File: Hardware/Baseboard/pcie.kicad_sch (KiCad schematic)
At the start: 1 part, among them J1 2199230-4

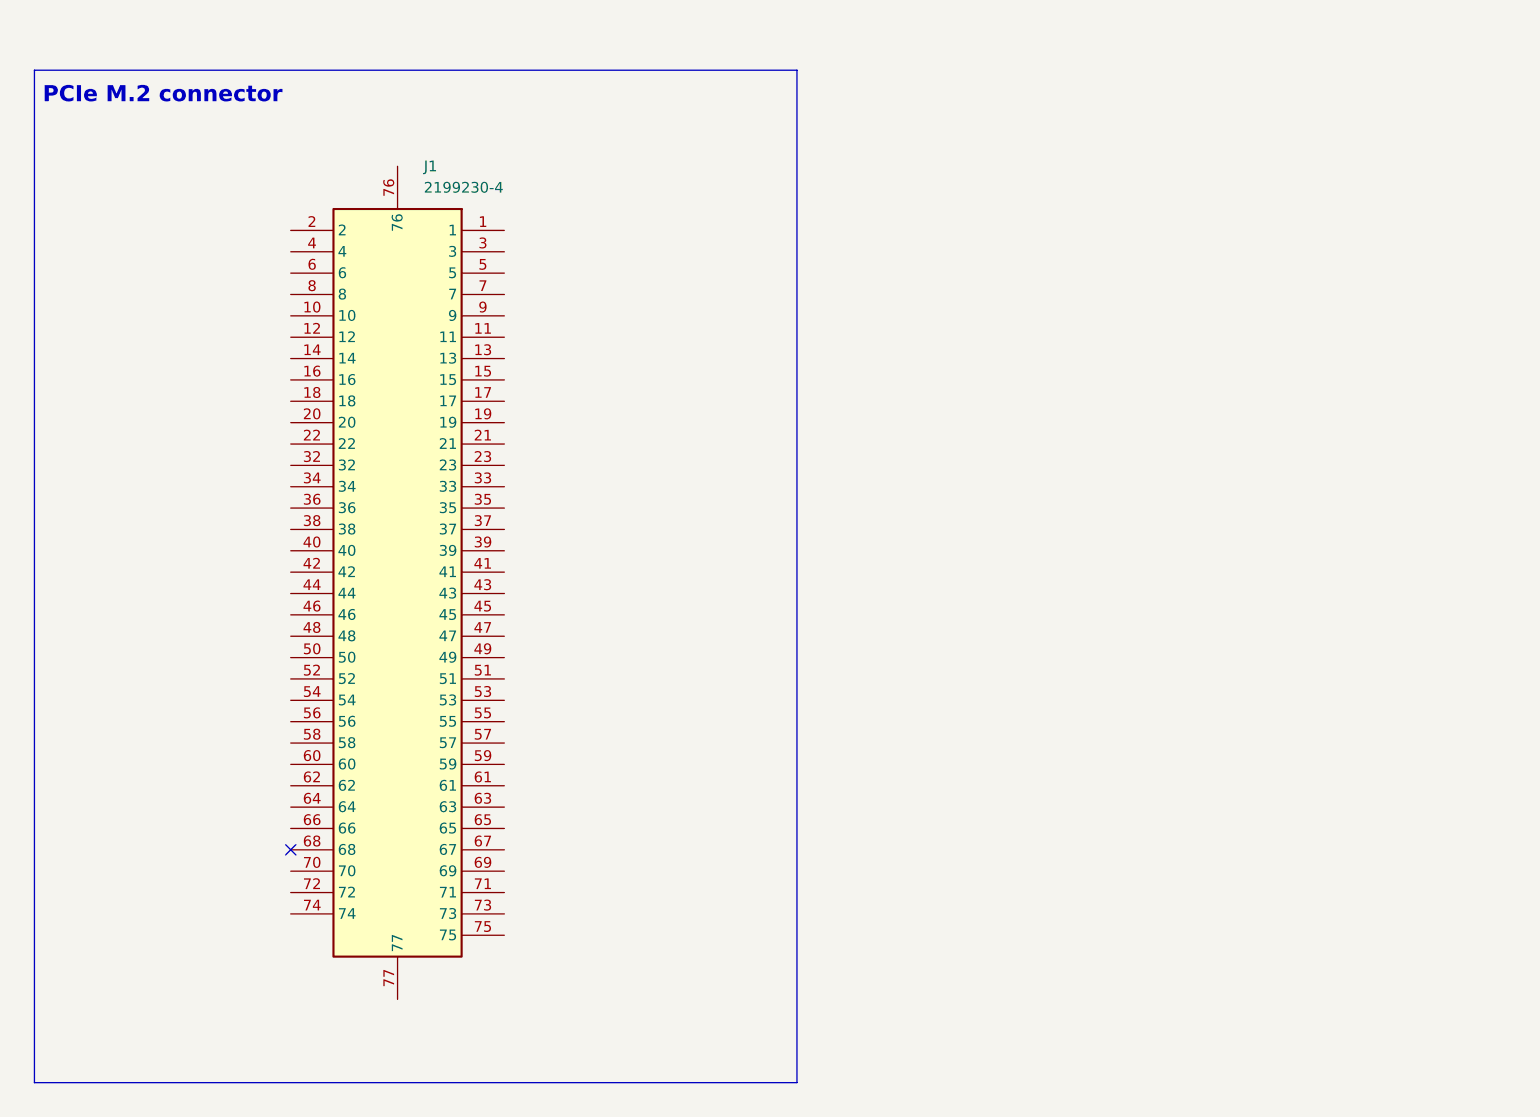
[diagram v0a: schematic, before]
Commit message: PCIe M.2 connector changed
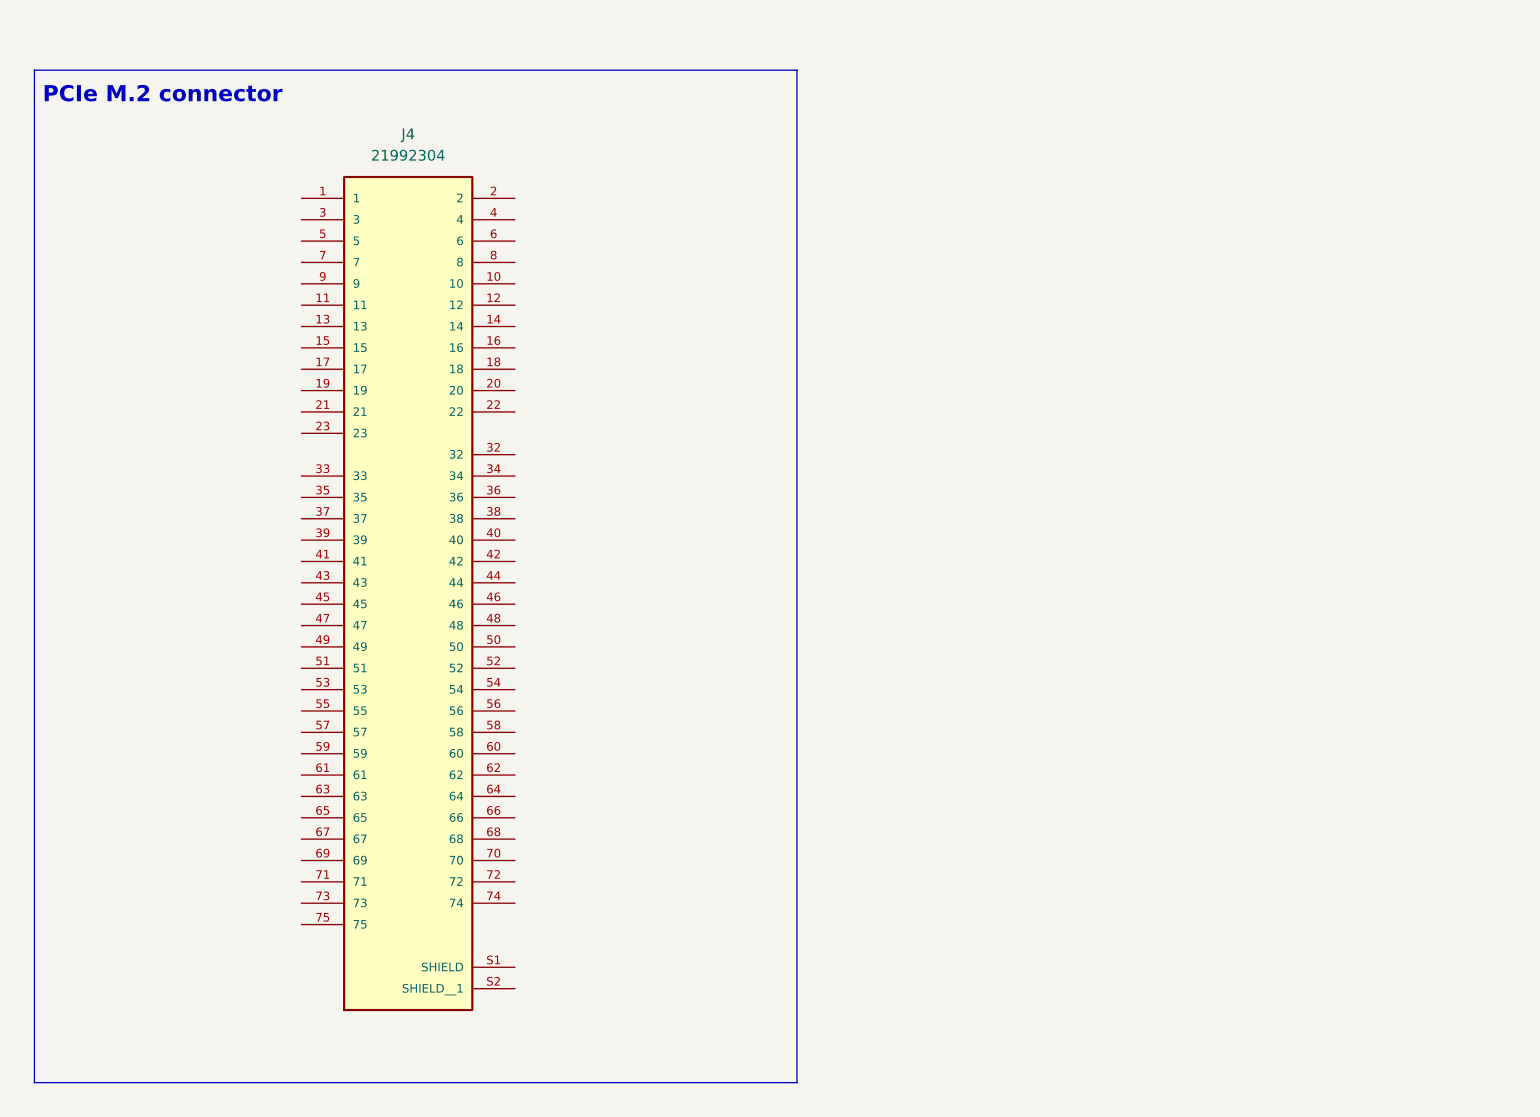
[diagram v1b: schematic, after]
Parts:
- removed J1: 2199230-4, FPGA4RISCV:21992304, symbol FPGA4RISCV:2199230-4
- added J4: 21992304, FPGA4RISCV:TE_21992304, symbol FPGA4RISCV:21992304
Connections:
- no-connect marks 1 -> 0
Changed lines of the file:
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@@
 		)
-	)
-	(no_connect
-		(at 78.74 125.73)
 	)
 	(symbol
-		(lib_id "FPGA4RISCV:2199230-4")
-		(at 91.44 44.45 270)
+		(lib_id "FPGA4RISCV:21992304")
+		(at 92.71 93.98 0)
 		(unit 1)
 		(exclude_from_sim no)
@@
 		(dnp no)
 		(fields_autoplaced yes)
-		(property "Reference" "J1"
-			(at 94.5581 44.45 90)
-			(effects
-				(font
-					(size 1.27 1.27)
-				)
-				(justify left)
-			)
-		)
-		(property "Value" "2199230-4"
-			(at 94.5581 46.99 90)
-			(effects
-				(font
-					(size 1.27 1.27)
-				)
-				(justify left)
-			)
-		)
-		(property "Footprint" "FPGA4RISCV:21992304"
-			(at 1.6 139.7 0)
-			(effects
-				(font
-					(size 1.27 1.27)
-				)
-				(justify left top)
-				(hide yes)
-			)
-		)
-		(property "Datasheet" "https://www.te.com/commerce/DocumentDelivery/DDEController?Action=srchrtrv&DocNm=1-1773706-1NGFF_QRG-SC&DocType=Data%20Sheet&DocLang=Chinese (Simplified)&PartCntxt=2199230-4&DocFormat=pdf"
-			(at -98.4 139.7 0)
-			(effects
-				(font
-					(size 1.27 1.27)
-				)
-				(justify left top)
-				(hide yes)
-			)
-		)
-		(property "Description" "Body Features: Primary Product Color Black | Connector & Keying Code E | Configuration Features: Number of Positions 67 | PCB Mount Orientation Right Angle | Number of Rows 2 | Contact Features: PCB Contact Termination Area Plating Material Tin | Contact Mating Area Plating Material Gold | Contact Mating Area Plating Material Thickness 15 MICIN | PCB Contact Termination Area Plating Material Finish Matte | PCB Contact Termination Area Plating Material Gold Flash | Contact Base Material Copper Alloy | Contac"
-			(at 91.44 44.45 0)
-			(effects
-				(font
-					(size 1.27 1.27)
-				)
-				(hide yes)
-			)
-		)
-		(property "Height" ""
-			(at -298.4 139.7 0)
-			(effects
-				(font
-					(size 1.27 1.27)
-				)
-				(justify left top)
-				(hide yes)
-			)
-		)
-		(property "Mouser Part Number" "571-2199230-4"
-			(at -398.4 139.7 0)
-			(effects
-				(font
-					(size 1.27 1.27)
-				)
-				(justify left top)
-				(hide yes)
-			)
-		)
-		(property "Mouser Price/Stock" "https://www.mouser.co.uk/ProductDetail/TE-Connectivity/2199230-4?qs=EQCnRgr4b6HnhitEoflgGQ%3D%3D"
-			(at -498.4 139.7 0)
-			(effects
-				(font
-					(size 1.27 1.27)
-				)
-				(justify left top)
-				(hide yes)
-			)
-		)
-		(property "Manufacturer_Name" "TE Connectivity"
-			(at -598.4 139.7 0)
-			(effects
-				(font
-					(size 1.27 1.27)
-				)
-				(justify left top)
-				(hide yes)
-			)
-		)
-		(property "Manufacturer_Part_Number" "2199230-4"
-			(at -698.4 139.7 0)
-			(effects
-				(font
-					(size 1.27 1.27)
-				)
-				(justify left top)
-				(hide yes)
-			)
+		(property "Reference" "J4"
+			(at 92.71 40.64 0)
+			(effects
+				(font
+					(size 1.27 1.27)
+				)
+			)
+		)
+		(property "Value" "21992304"
+			(at 92.71 43.18 0)
+			(effects
+				(font
+					(size 1.27 1.27)
+				)
+			)
+		)
+		(property "Footprint" "FPGA4RISCV:TE_21992304"
+			(at 92.71 93.98 0)
+			(effects
+				(font
+					(size 1.27 1.27)
+				)
+				(justify bottom)
+				(hide yes)
+			)
+		)
+		(property "Datasheet" ""
+			(at 92.71 93.98 0)
+			(effects
+				(font
+					(size 1.27 1.27)
+				)
+				(hide yes)
+			)
+		)
+		(property "Description" ""
+			(at 92.71 93.98 0)
+			(effects
+				(font
+					(size 1.27 1.27)
+				)
+				(hide yes)
+			)
+		)
+		(property "PARTREV" "B3"
+			(at 92.71 93.98 0)
+			(effects
+				(font
+					(size 1.27 1.27)
+				)
+				(justify bottom)
+				(hide yes)
+			)
+		)
+		(property "MAXIMUM_PACKAGE_HEIGHT" "4.2 mm"
+			(at 92.71 93.98 0)
+			(effects
+				(font
+					(size 1.27 1.27)
+				)
+				(justify bottom)
+				(hide yes)
+			)
+		)
+		(property "STANDARD" "Manufacturer recommendations"
+			(at 92.71 93.98 0)
+			(effects
+				(font
+					(size 1.27 1.27)
+				)
+				(justify bottom)
+				(hide yes)
+			)
+		)
+		(property "Manufacturer" "TE Connectivity"
+			(at 92.71 93.98 0)
+			(effects
+				(font
+					(size 1.27 1.27)
+				)
+				(justify bottom)
+				(hide yes)
+			)
+		)
+		(property "MPN" "2199230-4"
+			(at 92.71 93.98 0)
+			(effects
+				(font
+					(size 1.27 1.27)
+				)
+				(hide yes)
+			)
+		)
+		(pin "S1"
+		)
+		(pin "S2"
+		)
+		(pin "74"
+		)
+		(pin "72"
+		)
+		(pin "45"
+		)
+		(pin "57"
+		)
+		(pin "8"
+		)
+		(pin "42"
+		)
+		(pin "48"
+		)
+		(pin "63"
+		)
+		(pin "13"
+		)
+		(pin "67"
+		)
+		(pin "19"
+		)
+		(pin "16"
+		)
+		(pin "9"
+		)
+		(pin "46"
+		)
+		(pin "3"
+		)
+		(pin "2"
+		)
+		(pin "51"
+		)
+		(pin "20"
+		)
+		(pin "36"
+		)
+		(pin "11"
+		)
+		(pin "43"
+		)
+		(pin "35"
+		)
+		(pin "1"
+		)
+		(pin "23"
+		)
+		(pin "61"
+		)
+		(pin "7"
+		)
+		(pin "53"
+		)
+		(pin "59"
+		)
+		(pin "37"
+		)
+		(pin "69"
+		)
+		(pin "65"
+		)
+		(pin "47"
+		)
+		(pin "73"
+		)
+		(pin "49"
+		)
+		(pin "15"
+		)
+		(pin "5"
+		)
+		(pin "75"
+		)
+		(pin "4"
+		)
+		(pin "55"
+		)
+		(pin "6"
+		)
+		(pin "10"
+		)
+		(pin "12"
+		)
+		(pin "41"
+		)
+		(pin "14"
+		)
+		(pin "71"
+		)
+		(pin "22"
+		)
+		(pin "17"
 		)
 		(pin "32"
 		)
-		(pin "1"
-		)
-		(pin "19"
+		(pin "40"
 		)
 		(pin "21"
 		)
+		(pin "33"
+		)
+		(pin "39"
+		)
+		(pin "18"
+		)
 		(pin "34"
 		)
-		(pin "49"
-		)
-		(pin "15"
-		)
-		(pin "59"
-		)
-		(pin "61"
-		)
-		(pin "55"
-		)
 		(pin "38"
 		)
+		(pin "44"
+		)
 		(pin "50"
 		)
-		(pin "45"
+		(pin "52"
+		)
+		(pin "54"
+		)
+		(pin "56"
 		)
 		(pin "58"
 		)
-		(pin "57"
-		)
-		(pin "52"
-		)
-		(pin "56"
-		)
-		(pin "71"
-		)
-		(pin "39"
-		)
-		(pin "63"
+		(pin "60"
+		)
+		(pin "62"
+		)
+		(pin "64"
 		)
 		(pin "66"
 		)
-		(pin "12"
-		)
-		(pin "76"
-		)
-		(pin "10"
-		)
-		(pin "53"
-		)
-		(pin "67"
-		)
-		(pin "3"
-		)
-		(pin "4"
-		)
-		(pin "16"
-		)
-		(pin "22"
-		)
-		(pin "40"
-		)
-		(pin "5"
-		)
-		(pin "41"
-		)
-		(pin "43"
-		)
-		(pin "23"
-		)
-		(pin "20"
-		)
-		(pin "37"
-		)
-		(pin "36"
-		)
-		(pin "47"
-		)
-		(pin "6"
-		)
-		(pin "11"
-		)
-		(pin "2"
-		)
-		(pin "8"
-		)
-		(pin "9"
-		)
-		(pin "7"
-		)
-		(pin "33"
-		)
-		(pin "17"
-		)
-		(pin "18"
-		)
-		(pin "13"
-		)
-		(pin "14"
-		)
-		(pin "35"
-		)
-		(pin "42"
-		)
-		(pin "44"
-		)
-		(pin "46"
-		)
-		(pin "48"
-		)
-		(pin "51"
-		)
-		(pin "54"
-		)
-		(pin "60"
-		)
-		(pin "62"
-		)
-		(pin "64"
-		)
-		(pin "65"
-		)
 		(pin "68"
 		)
-		(pin "69"
-		)
 		(pin "70"
-		)
-		(pin "73"
-		)
-		(pin "74"
-		)
-		(pin "75"
-		)
-		(pin "77"
-		)
-		(pin "72"
 		)
 		(instances
 			(project ""
 				(path "/de32abb0-ff3b-4c67-a91a-eed08140b1b2/7b36eb32-e6b4-48cc-954e-a444a838f557"
-					(reference "J1")
+					(reference "J4")
 					(unit 1)
 				)

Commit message: BB: PCIe update
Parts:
- removed J4: 21992304, FPGA4RISCV:TE_21992304, symbol FPGA4RISCV:21992304
- added C18, C20, C21, C22, C24, C26, C27, C28: 100nF, Capacitor_SMD:C_0402_1005Metric, symbol RA8M1:885012205092
- added C19, C23, C25: 10uF, Capacitor_SMD:C_0402_1005Metric, symbol RA8M1:885012205092
- added J4: MDT275M02001, FPGA4RISCV:MDT275M02001, symbol FPGA4RISCV:MDT275M02001
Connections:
- new net +3.3V_PCIe: C18.2, C19.2, C20.2, C21.2, C22.2, C23.2, C24.2, C25.2, C26.2, C27.2, C28.2, J4.12, J4.14, J4.16, J4.18, J4.2, J4.4, J4.70, J4.72, J4.74
- new net CLKREQ#: J4.52
- new net GND: C18.1, C19.1, C20.1, C21.1, C22.1, C23.1, C24.1, C25.1, C26.1, C27.1, C28.1, J4.1, J4.15, J4.21, J4.27, J4.3, J4.33, J4.39, J4.45, J4.51, J4.57, J4.71, J4.73, J4.75, J4.76 (MP_1), J4.77 (MP_2), J4.9
- new net PCIe_CLK_N: J4.53
- new net PCIe_CLK_P: J4.55
- new net PCIe_RX0_N: J4.41
- new net PCIe_RX0_P: J4.43
- new net PCIe_RX1_N: J4.29
- new net PCIe_RX1_P: J4.31
- new net PCIe_RX2_N: J4.17
- new net PCIe_RX2_P: J4.19
- new net PCIe_RX3_N: J4.5
- new net PCIe_RX3_P: J4.7
- new net PCIe_TX0_N: J4.47
- new net PCIe_TX0_P: J4.49
- new net PCIe_TX1_N: J4.35
- new net PCIe_TX1_P: J4.37
- new net PCIe_TX2_N: J4.23
- new net PCIe_TX2_P: J4.25
- new net PCIe_TX3_N: J4.11
- new net PCIe_TX3_P: J4.13
- new net PERST#: J4.50
- no-connect marks 0 -> 24

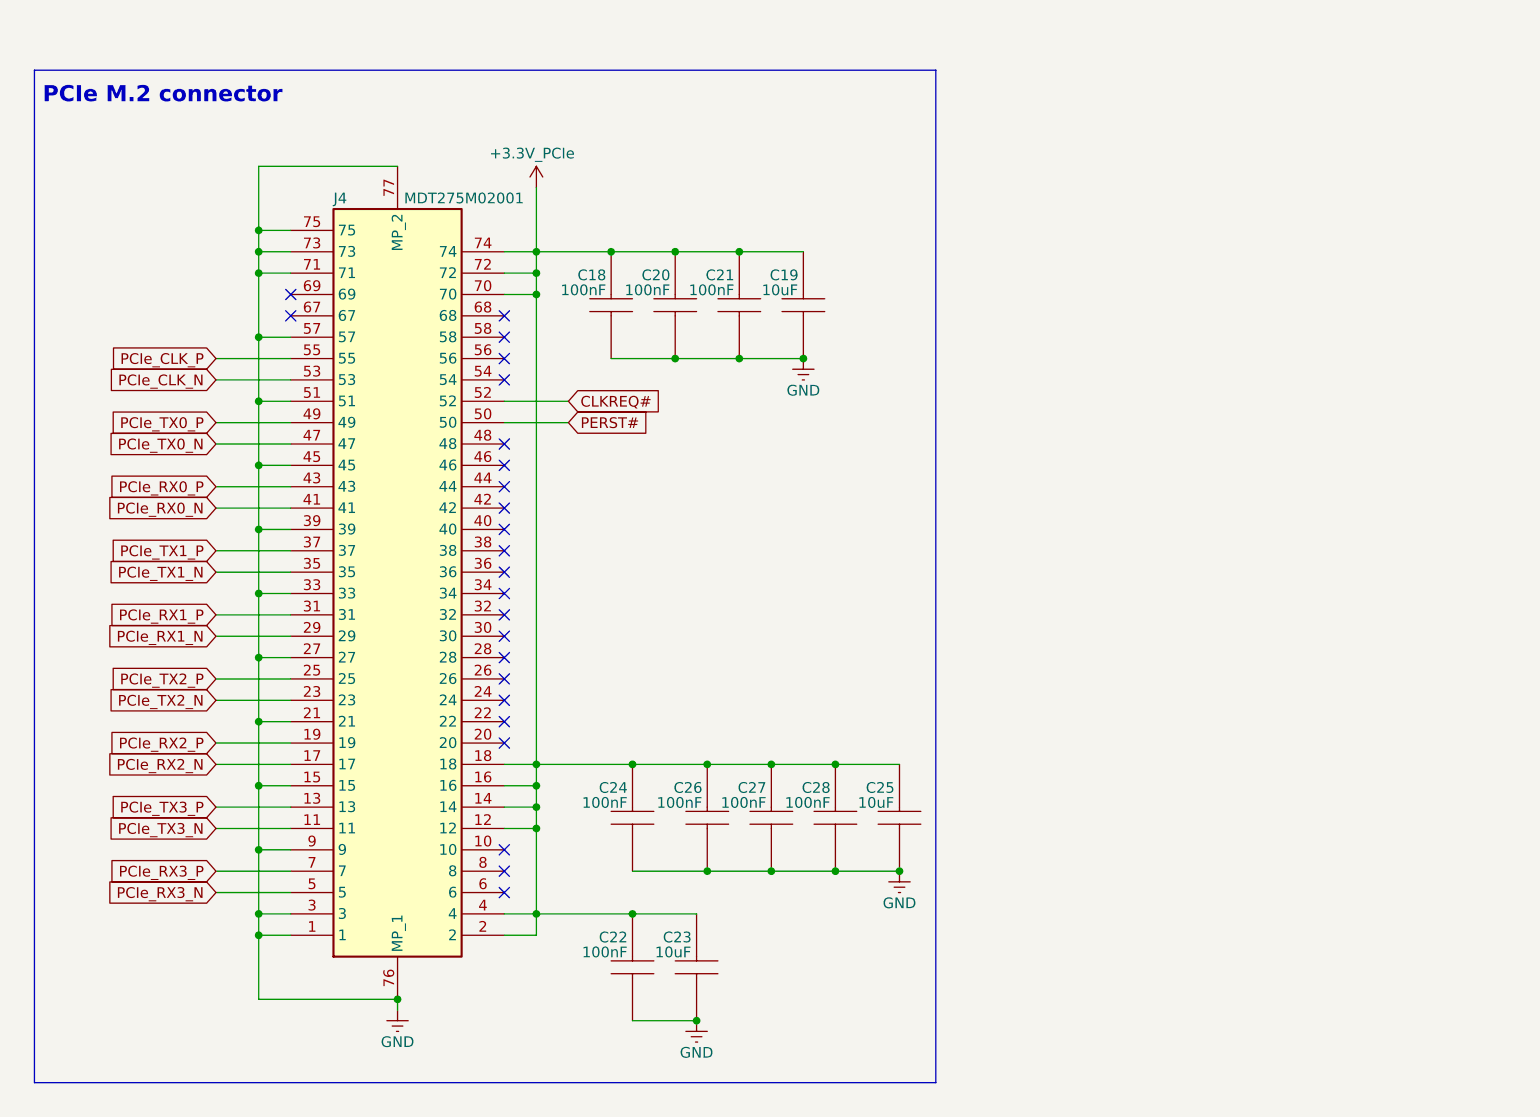
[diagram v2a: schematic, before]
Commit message: PCIe AC coupling
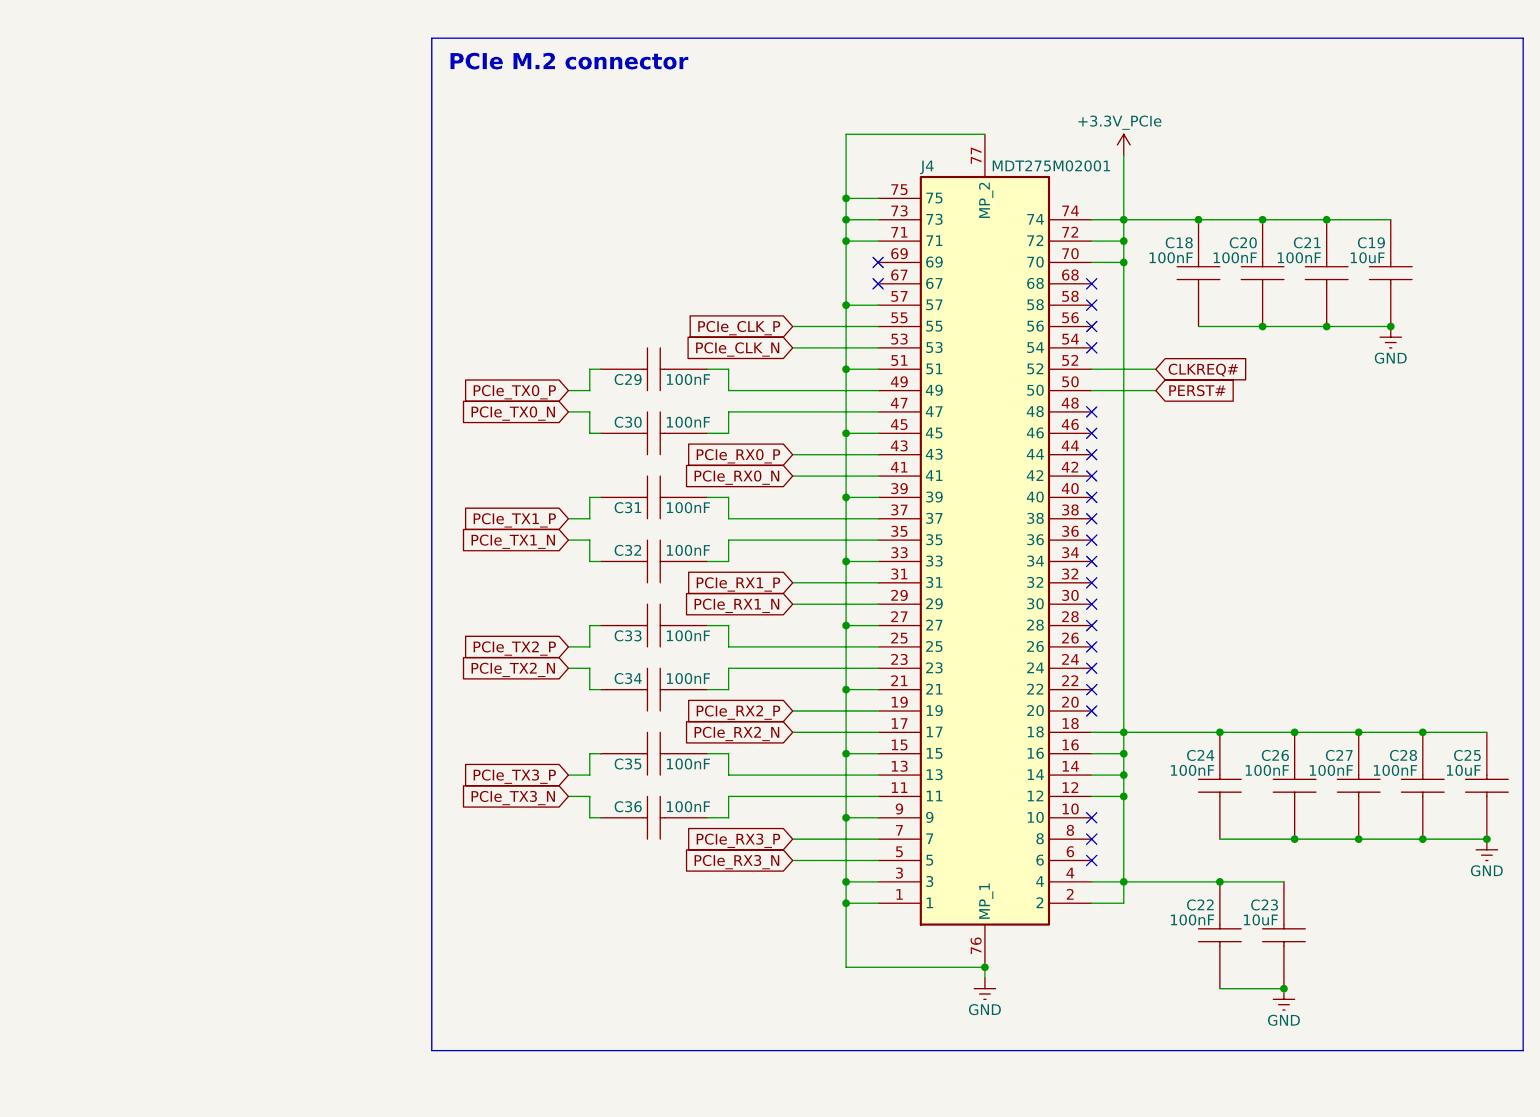
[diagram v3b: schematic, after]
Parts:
- added C29, C30, C31, C32, C33, C34, C35, C36: 100nF, Capacitor_SMD:C_0402_1005Metric, symbol RA8M1:885012205092
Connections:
- net PCIe_TX0_N: now also C30.2; no longer J4.47
- net PCIe_TX0_P: now also C29.2; no longer J4.49
- net PCIe_TX1_N: now also C32.2; no longer J4.35
- net PCIe_TX1_P: now also C31.2; no longer J4.37
- net PCIe_TX2_N: now also C34.2; no longer J4.23
- net PCIe_TX2_P: now also C33.2; no longer J4.25
- net PCIe_TX3_N: now also C36.2; no longer J4.11
- net PCIe_TX3_P: now also C35.2; no longer J4.13
- new net: C36.1, J4.11
- new net: C35.1, J4.13
- new net: C34.1, J4.23
- new net: C33.1, J4.25
- new net: C32.1, J4.35
- new net: C31.1, J4.37
- new net: C30.1, J4.47
- new net: C29.1, J4.49
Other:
- moved on the sheet: C18, C19, C20, C21, C22, C23, C24, C25, C26, C27, C28, J4
